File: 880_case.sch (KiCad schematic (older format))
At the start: 163 parts, among them CON1 BARREL_JACK, J1 RUN/STOP, J10 RS IN, J11 CP IN, J12 MA IN, J13 CB IN, J14 CY IN, J15 OH IN, J16 CH IN, J17 IN 1, J18 IN 2, J19 IN 3, J2 SYNC24 CLK, J20 IN 4, J21 MULT IN, J22 SUM, J23 JACK_STEREO, J3 ASSIGN 1, J4 ASSIGN 2, J5 BD IN, J6 SD IN, J7 LT IN, J8 MT IN, J9 HT IN, P1 CONN_02X03, P2 CONN_01X02, P3 CONN_02X05, P4 CONN_01X03, Q1 MMBT3904, Q10 MMBT3904, Q11 MMBT3904, Q12 MMBT3904, Q13 MMBT3904, Q14 C945, Q15 A733, Q2 MMBT3904, Q3 MMBT3904, Q4 MMBT3904, Q5 MMBT3904, Q6 MMBT3904, Q7 MMBT3904, Q8 MMBT3904, Q9 MMBT3904, U1 74HC165, U2 74HC165, U3 VX078-500, U4 VX078-500, U5 4558, U6 4558, X1 MIDI OUT, X2 SYNC24

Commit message: first route complete
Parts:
- removed TP3: CONN_1, MyModules:TEST_POINT_LOOP_4592, symbol CONN_1
- added R65, R66: 0R, MyModules:SM0603-R-YAGEO, symbol R_US
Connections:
- net GND: now also R65.2, R66.2
- net ~CE: now also R65.1, R66.1
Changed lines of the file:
@@
 $EndComp
 $Comp
-L CONN_1 TP3
-U 1 1 5C480538
-P 18775 11025
-F 0 "TP3" V 18925 10975 60  0000 L CNN
-F 1 "CONN_1" H 18775 11080 30  0001 C CNN
-F 2 "MyModules:TEST_POINT_LOOP_4592" H 18775 11025 60  0001 C CNN
-F 3 "" H 18775 11025 60  0000 C CNN
-	1    18775 11025
-	0    -1   -1   0
-$EndComp
-$Comp
-L GND_E #PWR04
-U 1 1 5C48053F
-P 18775 11325
-F 0 "#PWR04" V 18775 11325 30  0001 C CNN
-F 1 "GND_E" H 18775 11255 30  0001 C CNN
-F 2 "~" H 18775 11325 60  0000 C CNN
-F 3 "~" H 18775 11325 60  0000 C CNN
-	1    18775 11325
-	1    0    0    -1
-$EndComp
-$Comp
 L CONN_02X03 ISP1
 U 1 1 5C480545
@@
 Wire Wire Line
 	18475 11175 18475 11325
-Wire Wire Line
-	18775 11175 18775 11325
 Connection ~ 19150 11825
 Wire Wire Line
@@
 NoConn ~ 17950 7575
 NoConn ~ 17950 7675
+$Comp
+L R_US R66
+U 1 1 5C5771F9
+P 17125 10275
+F 0 "R66" H 16975 10400 50  0000 C CNN
+F 1 "0R" H 17000 10325 50  0000 C CNN
+F 2 "MyModules:SM0603-R-YAGEO" H 17125 10275 60  0001 C CNN
+F 3 "~" H 17125 10275 60  0000 C CNN
+	1    17125 10275
+	-1   0    0    -1
+$EndComp
+$Comp
+L R_US R65
+U 1 1 5C577FC2
+P 16825 10275
+F 0 "R65" H 16675 10400 50  0000 C CNN
+F 1 "0R" H 16700 10325 50  0000 C CNN
+F 2 "MyModules:SM0603-R-YAGEO" H 16825 10275 60  0001 C CNN
+F 3 "~" H 16825 10275 60  0000 C CNN
+	1    16825 10275
+	-1   0    0    -1
+$EndComp
+Text Label 16825 10000 0    60   ~ 0
+~CE
+Wire Wire Line
+	16825 10000 16825 10075
+Text Label 17125 10000 0    60   ~ 0
+~CE
+Wire Wire Line
+	17125 10000 17125 10075
+$Comp
+L GND_E #PWR094
+U 1 1 5C578C93
+P 16825 10550
+F 0 "#PWR094" V 16825 10550 30  0001 C CNN
+F 1 "GND_E" H 16825 10480 30  0001 C CNN
+F 2 "~" H 16825 10550 60  0000 C CNN
+F 3 "~" H 16825 10550 60  0000 C CNN
+	1    16825 10550
+	-1   0    0    -1
+$EndComp
+Wire Wire Line
+	16825 10550 16825 10475
+$Comp
+L GND_E #PWR095
+U 1 1 5C5790FF
+P 17125 10550
+F 0 "#PWR095" V 17125 10550 30  0001 C CNN
+F 1 "GND_E" H 17125 10480 30  0001 C CNN
+F 2 "~" H 17125 10550 60  0000 C CNN
+F 3 "~" H 17125 10550 60  0000 C CNN
+	1    17125 10550
+	-1   0    0    -1
+$EndComp
+Wire Wire Line
+	17125 10550 17125 10475
 $EndSCHEMATC

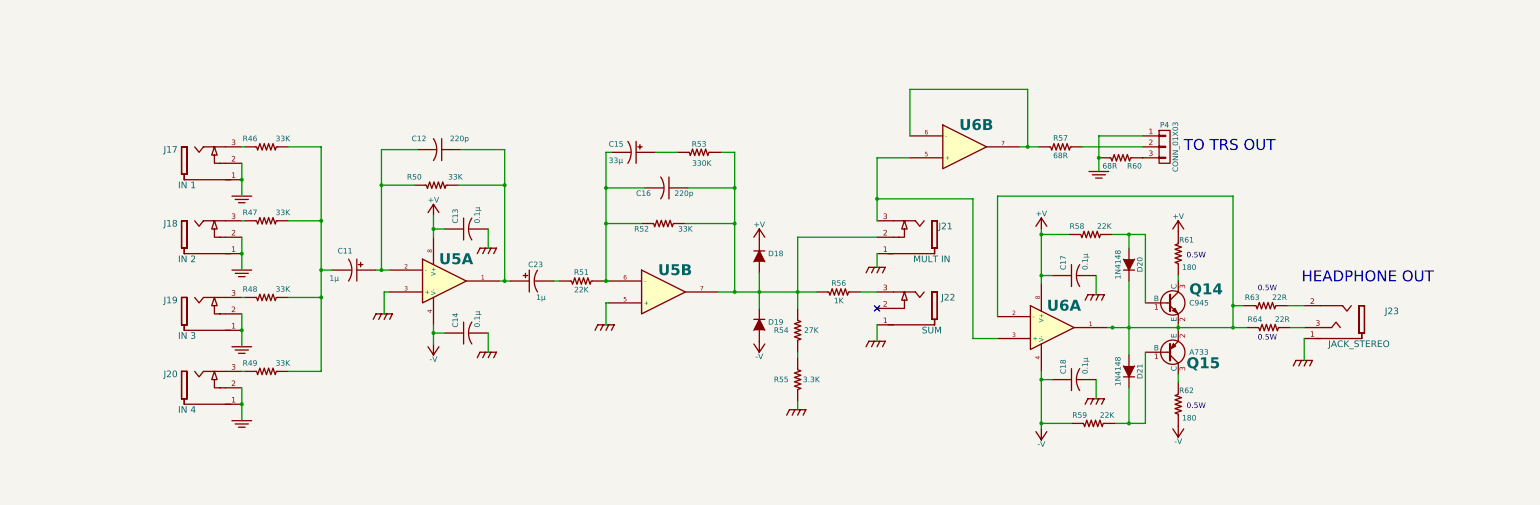
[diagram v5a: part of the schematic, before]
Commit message: added insert on submix sum. put insert jack and headphone jack on daughter board
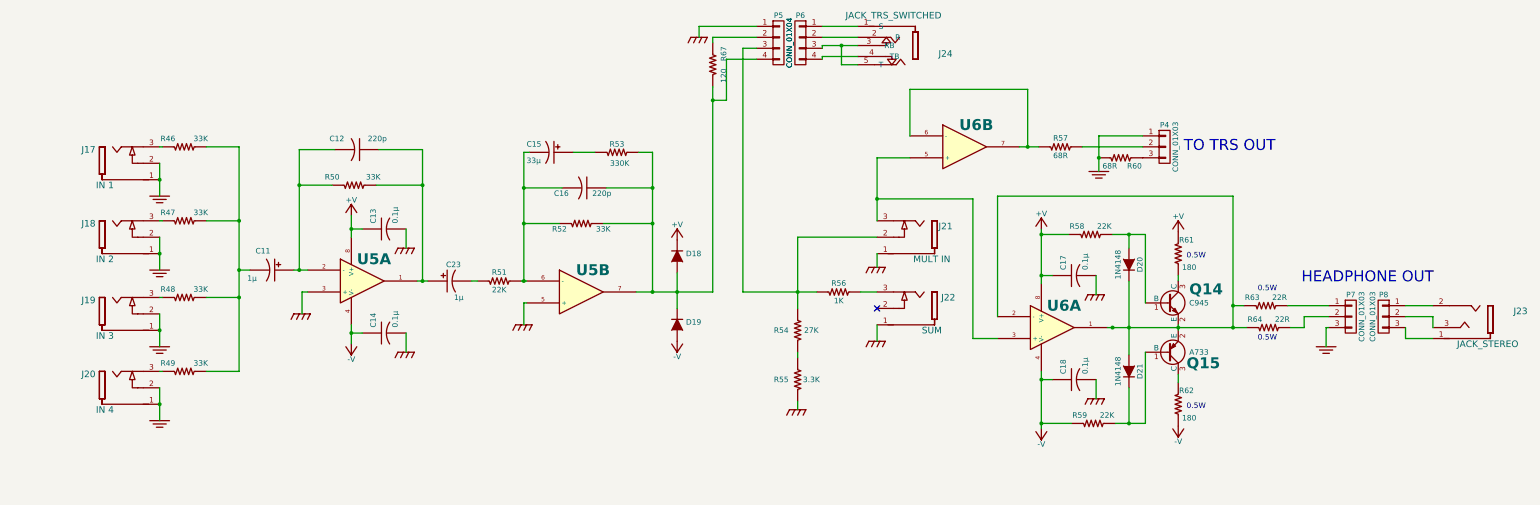
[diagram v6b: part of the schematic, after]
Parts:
- added J24: JACK_TRS_SWITCHED, MyModules:RA49B14B_SWITCHCRAFT, symbol JACK_TRS_SWITCHED
- added P5, P6: CONN_01X04, Pin_Headers:Pin_Header_Straight_1x04_Pitch2.54mm, symbol CONN_01X04
- added P7, P8: CONN_01X03, Pin_Headers:Pin_Header_Straight_1x03_Pitch2.54mm, symbol CONN_01X03
- added R67: 120, Resistors_SMD:R_0805, symbol R_US
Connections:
- net GND: now also P5.1 (P1), P7.3 (P3); no longer J23.1
- net at C16.1, D18.2 (A), D19.1 (K)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: now also P5.4 (P4), R67.1; no longer J21.2, R54.2, R56.2
- net at J23.2: now also P8.1 (P1); no longer R63.2
- net at J23.3: now also P8.2 (P2); no longer R64.2
- new net: J23.1, P8.3 (P3)
- new net: P7.1 (P1), R63.2
- new net: P7.2 (P2), R64.2
- new net: J21.2, P5.3 (P3), R54.2, R56.2
- new net: J24.1 (S), P6.1 (P1)
- new net: J24.2 (R), P6.2 (P2)
- new net: J24.3 (RB), J24.5 (T), P6.3 (P3)
- new net: J24.4 (TB), P6.4 (P4)
- new net: P5.2 (P2), R67.2
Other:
- moved on the sheet: C11, C12, C13, C14, C15, C16, C23, D18, D19, J17, J18, J19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

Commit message: first prototype PCB ordered
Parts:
- removed R65, R66: 0R, MyModules:SM0603-R-YAGEO, symbol R_US
- added P9: CONN_01X03, Pin_Headers:Pin_Header_Straight_1x03_Pitch2.54mm, symbol CONN_01X03
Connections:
- net GND: now also U2.3 (D4), U2.4 (D5), U2.5 (D6), P9.1 (P1)
- net ~CE: now also P9.2 (P2); no longer Q13.3 (C), R45.2
- new net: P9.3 (P3), Q13.3 (C), R45.2
- no-connect marks 18 -> 14
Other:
- note added: "Input protection is on\nmain 880 board"
- note added: "Is pull-up here\nreally necessary?\nMay cause trouble with \nreset, delete or increase?"
- note added: "Probably want to tri-state\n74HC165s during ISP programming.\nJumper makes this optional"
- note added: "USE ISP_MOSI as LATCH"
- note removed: "Probably want to tri-state 74HC165s \nduring ISP programming. Maybe not?"

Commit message: working on second revision, about to move headhpone amp circuit to align board-to-board connectors
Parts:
- P3: value CONN_02X05 -> CONN_02X08; symbol CONN_02X05 -> CONN_02X08
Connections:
- net GND: now also U2.6 (D7)
- no-connect marks 14 -> 20
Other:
- note added: "TRS SWITCHED PIN OUT WRONG - FIX!"
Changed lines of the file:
@@
 Connection ~ 3250 7625
 $Comp
-L CONN_02X05 P3
+L CONN_02X08 P3
 U 1 1 5C4A3DA7
-P 20625 12675
-F 0 "P3" H 20625 12975 50  0000 C CNN
-F 1 "CONN_02X05" H 20625 12375 50  0000 C CNN
-F 2 "w_conn_strip:vasch_strip_5x2" H 20625 11475 60  0001 C CNN
-F 3 "" H 20625 11475 60  0000 C CNN
-	1    20625 12675
+P 20625 12525
+F 0 "P3" H 20625 12825 50  0000 C CNN
+F 1 "CONN_02X08" H 20625 12025 50  0000 C CNN
+F 2 "w_conn_strip:vasch_strip_5x2" H 20625 11325 60  0001 C CNN
+F 3 "" H 20625 11325 60  0000 C CNN
+	1    20625 12525
 	-1   0    0    1
 $EndComp
@@
 Connection ~ 20875 12675
 Wire Wire Line
-	20875 12125 20875 12475
-Wire Wire Line
 	20875 13200 20875 12875
 Wire Wire Line
@@
 Connection ~ 20375 12675
 Wire Wire Line
-	20300 12125 20875 12125
+	19900 11825 20950 11825
 Wire Wire Line
 	20300 13200 20875 13200
@@
 $EndComp
 Wire Wire Line
-	19900 11825 20300 11825
-Wire Wire Line
 	20000 11675 20000 12025
 $Comp
@@
 Connection ~ 15775 11825
 Wire Wire Line
+	20300 11825 20300 11825
+Wire Wire Line
 	20300 11825 20300 12475
 Text GLabel 14175 7200 0    50   BiDi ~ 0
@@
 Wire Wire Line
 	20300 12475 20375 12475
-Connection ~ 20300 12125
+Connection ~ 20300 11825
 $Comp
 L D_Schottky D17
@@
 	-1   0    0    1
 $EndComp
-Connection ~ 18575 4075
 $Comp
 L C_US C18
@@
 L PWR_FLAG #FLG088
 U 1 1 5C53C1B3
-P 20875 12125
-F 0 "#FLG088" H 20875 12220 50  0001 C CNN
-F 1 "PWR_FLAG" H 20875 12305 50  0000 C CNN
-F 2 "" H 20875 12125 60  0000 C CNN
-F 3 "" H 20875 12125 60  0000 C CNN
-	1    20875 12125
+P 20875 11825
+F 0 "#FLG088" H 20875 11920 50  0001 C CNN
+F 1 "PWR_FLAG" H 20875 12005 50  0000 C CNN
+F 2 "" H 20875 11825 60  0000 C CNN
+F 3 "" H 20875 11825 60  0000 C CNN
+	1    20875 11825
 	1    0    0    -1
 $EndComp
@@
 $EndComp
 Connection ~ 21175 12675
-Connection ~ 20875 12125
+Connection ~ 20875 11825
 $Comp
 L PWR_FLAG #FLG090
@@
 Connection ~ 18325 7575
 Wire Wire Line
-	17975 7675 18325 7675
+	17950 7675 18325 7675
 Connection ~ 18325 7675
 Text Notes 1725 3925 2    60   ~ 0
 Input protection is on\nmain 880 board
+Text Notes 14850 1100 0    100  ~ 0
+TRS SWITCHED PIN OUT WRONG - FIX!
+Wire Wire Line
+	20875 12475 20950 12475
+Wire Wire Line
+	20950 12475 20950 11825
+NoConn ~ 20375 12175
+NoConn ~ 20375 12275
+NoConn ~ 20375 12375
+NoConn ~ 20875 12175
+NoConn ~ 20875 12275
+NoConn ~ 20875 12375
 $EndSCHEMATC
